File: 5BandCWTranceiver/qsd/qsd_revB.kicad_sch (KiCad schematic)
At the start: 56 parts, among them IC1 MCP1801, IC2 SN74LVC1G04DBVT, IC3 SN74AUP2G79DCUR, IC4 TS5A23157, IC5 SN74CBTLV3253, IC6 SN74LVC1G04DBVT, J1 Conn_Coaxial, J2 Conn_Coaxial, J3 Conn_Coaxial, Q1 J309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

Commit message: Update Audio Board
modify design and layout improvements
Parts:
- C12, C13, C14, C15: value 0.15uF -> 0.22uF
- R8: value 4.7k -> 4.32K
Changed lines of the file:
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@@
       (effects (font (size 1.778 1.5113)) (justify left bottom))
     )
-    (property "Value" "0.15uF" (id 1) (at 289.56 111.76 90)
+    (property "Value" "0.22uF" (id 1) (at 289.56 111.76 90)
       (effects (font (size 1.778 1.5113)) (justify left bottom))
     )
@@
       (effects (font (size 1.778 1.5113)) (justify left bottom))
     )
-    (property "Value" "0.15uF" (id 1) (at 274.32 111.76 90)
+    (property "Value" "0.22uF" (id 1) (at 274.32 111.76 90)
       (effects (font (size 1.778 1.5113)) (justify left bottom))
     )
@@
     (pin "2")
     (pin "3")
+    (pin "5")
+    (pin "6")
+    (pin "7")
+    (pin "4")
+    (pin "8")
   )
   (symbol (lib_id "qsd_revB-eagle-import:CAP0603-CAP") (at 264.16 134.62 180) (unit 1)
@@
       (effects (font (size 1.27 1.27)) hide)
     )
+    (pin "1")
+    (pin "2")
+    (pin "3")
     (pin "5")
     (pin "6")
     (pin "7")
+    (pin "4")
+    (pin "8")
   )
   (symbol (lib_id "qsd_revB-eagle-import:SN74LVC1G04DBVT") (at 111.76 167.64 0) (mirror y) (unit 1)
@@
       (effects (font (size 1.778 1.5113)) (justify left bottom))
     )
-    (property "Value" "0.15uF" (id 1) (at 297.18 111.76 90)
+    (property "Value" "0.22uF" (id 1) (at 297.18 111.76 90)
       (effects (font (size 1.778 1.5113)) (justify left bottom))
     )
@@
       (effects (font (size 1.778 1.5113)) (justify left bottom))
     )
-    (property "Value" "0.15uF" (id 1) (at 281.94 111.76 90)
+    (property "Value" "0.22uF" (id 1) (at 281.94 111.76 90)
       (effects (font (size 1.778 1.5113)) (justify left bottom))
     )
@@
       (effects (font (size 1.27 1.27)) hide)
     )
+    (pin "1")
+    (pin "2")
+    (pin "3")
+    (pin "5")
+    (pin "6")
+    (pin "7")
     (pin "4")
     (pin "8")
@@
       (effects (font (size 1.778 1.5113)) (justify left bottom))
     )
-    (property "Value" "4.7k" (id 1) (at 183.642 74.422 90)
+    (property "Value" "4.32K" (id 1) (at 183.642 74.422 90)
       (effects (font (size 1.778 1.5113)) (justify left bottom))
     )
@@
     )
     (path "/34e7dd80-c472-473e-a03d-21ea2317bbb8"
-      (reference "C12") (unit 1) (value "0.15uF") (footprint "Capacitor_SMD:C_0603_1608Metric_Pad1.08x0.95mm_HandSolder")
+      (reference "C12") (unit 1) (value "0.22uF") (footprint "Capacitor_SMD:C_0603_1608Metric_Pad1.08x0.95mm_HandSolder")
     )
     (path "/a8fd90c3-93bd-4d70-a767-e358a34a4f2a"
-      (reference "C13") (unit 1) (value "0.15uF") (footprint "Capacitor_SMD:C_0603_1608Metric_Pad1.08x0.95mm_HandSolder")
+      (reference "C13") (unit 1) (value "0.22uF") (footprint "Capacitor_SMD:C_0603_1608Metric_Pad1.08x0.95mm_HandSolder")
     )
     (path "/31c0c5d6-f2fd-4c78-836e-b4282fb318e1"
-      (reference "C14") (unit 1) (value "0.15uF") (footprint "Capacitor_SMD:C_0603_1608Metric_Pad1.08x0.95mm_HandSolder")
+      (reference "C14") (unit 1) (value "0.22uF") (footprint "Capacitor_SMD:C_0603_1608Metric_Pad1.08x0.95mm_HandSolder")
     )
     (path "/59cf1f4c-3c5e-4212-a0d9-c5ed9febcb10"
-      (reference "C15") (unit 1) (value "0.15uF") (footprint "Capacitor_SMD:C_0603_1608Metric_Pad1.08x0.95mm_HandSolder")
+      (reference "C15") (unit 1) (value "0.22uF") (footprint "Capacitor_SMD:C_0603_1608Metric_Pad1.08x0.95mm_HandSolder")
     )
     (path "/bac4bbf2-6a2f-46b1-b0c0-bf58806b4d24"
@@
     )
     (path "/ea505101-ccf9-4547-a897-6133e97a8a41"
-      (reference "R8") (unit 1) (value "4.7k") (footprint "Resistor_SMD:R_0603_1608Metric_Pad0.98x0.95mm_HandSolder")
+      (reference "R8") (unit 1) (value "4.32K") (footprint "Resistor_SMD:R_0603_1608Metric_Pad0.98x0.95mm_HandSolder")
     )
     (path "/e77cdba9-df1d-409f-b12f-bec7ebba09c1"

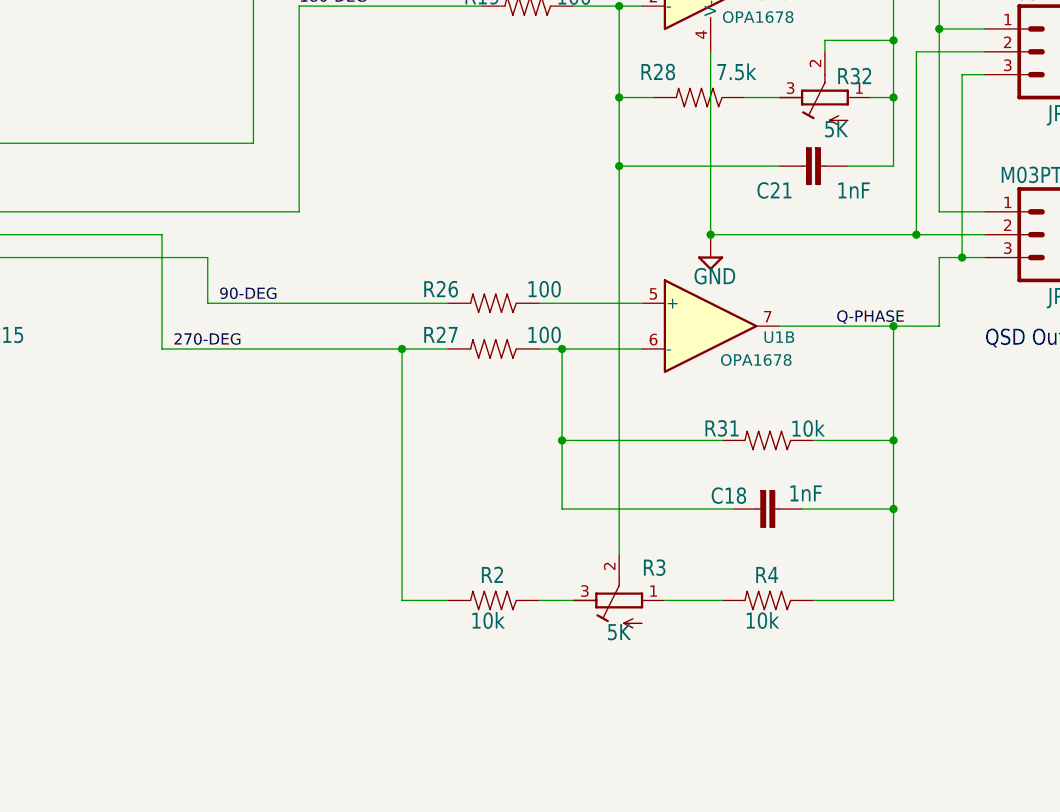
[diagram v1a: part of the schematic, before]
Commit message: Tapeout - audio and power boards
Last mods to audio board; new power board
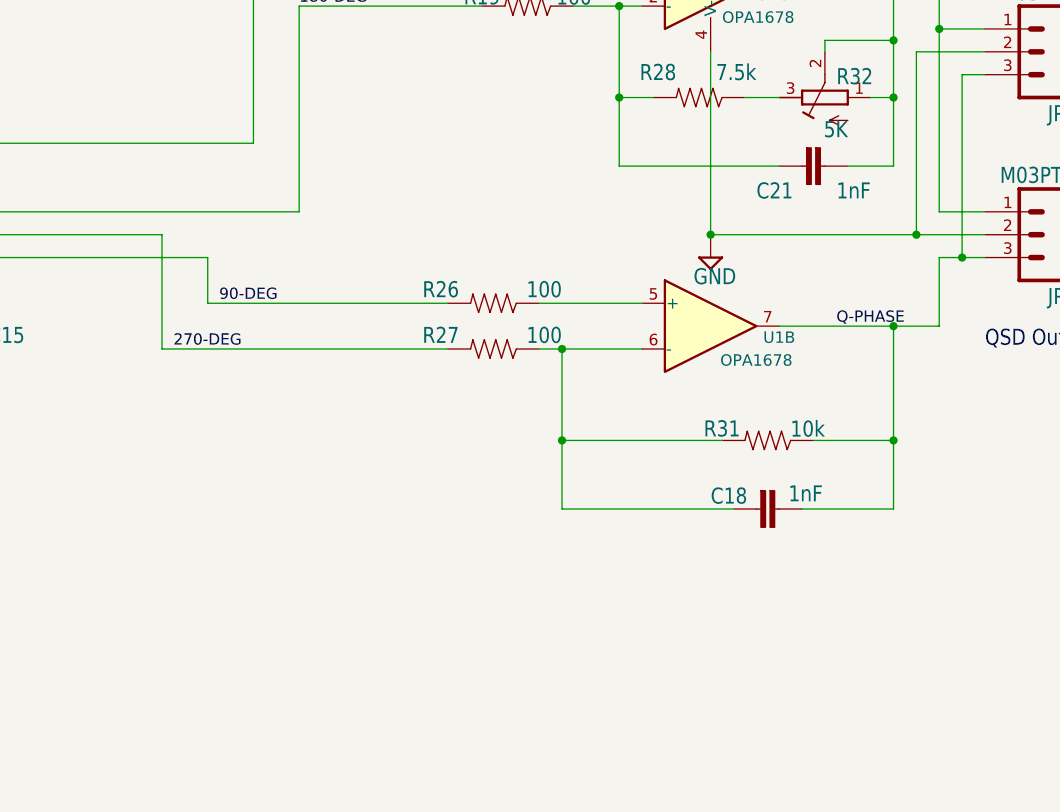
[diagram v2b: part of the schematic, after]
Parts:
- removed R2, R4: 10k, Resistor_SMD:R_0603_1608Metric_Pad0.98x0.95mm_HandSolder, symbol qsd_revB-eagle-import:RESISTOR0603-RES
- removed R3: 5K, qsd_revB:RTRIM3296W, symbol qsd_revB-eagle-import:R-TRIMM3296W
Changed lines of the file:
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@@
   (junction (at 116.84 154.94) (diameter 0) (color 0 0 0 0)
   )
-  (junction (at 368.3 88.9) (diameter 0) (color 0 0 0 0)
-  )
   (junction (at 152.4 139.7) (diameter 0) (color 0 0 0 0)
   )
@@
   (junction (at 266.7 83.82) (diameter 0) (color 0 0 0 0)
   )
-  (junction (at 398.78 127) (diameter 0) (color 0 0 0 0)
-  )
   (junction (at 398.78 106.68) (diameter 0) (color 0 0 0 0)
   )
@@
   (junction (at 274.32 86.36) (diameter 0) (color 0 0 0 0)
   )
-  (junction (at 344.17 109.22) (diameter 0) (color 0 0 0 0)
-  )
   (junction (at 45.72 33.02) (diameter 0) (color 0 0 0 0)
   )
@@
     (stroke (width 0) (type default) (color 0 0 0 0))
   )
-  (wire (pts (xy 368.3 88.9) (xy 368.3 132.08))
-    (stroke (width 0) (type default) (color 0 0 0 0))
-  )
   (wire (pts (xy 180.34 144.78) (xy 170.18 144.78))
     (stroke (width 0) (type default) (color 0 0 0 0))
@@
     (stroke (width 0) (type default) (color 0 0 0 0))
   )
-  (wire (pts (xy 359.41 137.16) (xy 363.22 137.16))
-    (stroke (width 0) (type default) (color 0 0 0 0))
-  )
   (wire (pts (xy 40.64 50.8) (xy 45.72 50.8))
     (stroke (width 0) (type default) (color 0 0 0 0))
@@
     (stroke (width 0) (type default) (color 0 0 0 0))
   )
-  (wire (pts (xy 373.38 137.16) (xy 379.73 137.16))
-    (stroke (width 0) (type default) (color 0 0 0 0))
-  )
   (wire (pts (xy 210.82 180.34) (xy 187.96 180.34))
     (stroke (width 0) (type default) (color 0 0 0 0))
@@
     (stroke (width 0) (type default) (color 0 0 0 0))
   )
-  (wire (pts (xy 317.5 109.22) (xy 344.17 109.22))
+  (wire (pts (xy 317.5 109.22) (xy 349.25 109.22))
     (stroke (width 0) (type default) (color 0 0 0 0))
   )
@@
     (stroke (width 0) (type default) (color 0 0 0 0))
   )
-  (wire (pts (xy 344.17 109.22) (xy 349.25 109.22))
-    (stroke (width 0) (type default) (color 0 0 0 0))
-  )
   (wire (pts (xy 147.32 144.78) (xy 154.94 144.78))
     (stroke (width 0) (type default) (color 0 0 0 0))
@@
     (stroke (width 0) (type default) (color 0 0 0 0))
   )
-  (wire (pts (xy 344.17 137.16) (xy 344.17 109.22))
-    (stroke (width 0) (type default) (color 0 0 0 0))
-  )
   (wire (pts (xy 105.41 208.28) (xy 105.41 193.04))
     (stroke (width 0) (type default) (color 0 0 0 0))
@@
     (stroke (width 0) (type default) (color 0 0 0 0))
   )
-  (wire (pts (xy 389.89 137.16) (xy 398.78 137.16))
-    (stroke (width 0) (type default) (color 0 0 0 0))
-  )
   (wire (pts (xy 266.7 93.98) (xy 264.16 93.98))
     (stroke (width 0) (type default) (color 0 0 0 0))
@@
     (stroke (width 0) (type default) (color 0 0 0 0))
   )
-  (wire (pts (xy 344.17 137.16) (xy 349.25 137.16))
-    (stroke (width 0) (type default) (color 0 0 0 0))
-  )
   (wire (pts (xy 398.78 106.68) (xy 386.08 106.68))
     (stroke (width 0) (type default) (color 0 0 0 0))
@@
   )
   (wire (pts (xy 403.86 45.72) (xy 403.86 48.26))
-    (stroke (width 0) (type default) (color 0 0 0 0))
-  )
-  (wire (pts (xy 398.78 137.16) (xy 398.78 127))
     (stroke (width 0) (type default) (color 0 0 0 0))
   )
@@
     (pin "2")
   )
-  (symbol (lib_id "qsd_revB-eagle-import:R-TRIMM3296W") (at 368.3 137.16 90) (unit 1)
-    (in_bom yes) (on_board yes)
-    (property "Reference" "R3" (id 0) (at 370.84 134.62 90)
-      (effects (font (size 1.778 1.5113)) (justify right top))
-    )
-    (property "Value" "5K" (id 1) (at 369.57 139.7 90)
-      (effects (font (size 1.778 1.5113)) (justify left bottom))
-    )
-    (property "Footprint" "qsd_revB:RTRIM3296W" (id 2) (at 368.3 137.16 0)
-      (effects (font (size 1.27 1.27)) hide)
-    )
-    (property "Datasheet" "" (id 3) (at 368.3 137.16 0)
-      (effects (font (size 1.27 1.27)) hide)
-    )
-    (pin "1")
-    (pin "2")
-    (pin "3")
-  )
   (symbol (lib_id "qsd_revB-eagle-import:GND") (at 45.72 88.9 0) (unit 1)
     (in_bom yes) (on_board yes)
@@
     (pin "2")
   )
-  (symbol (lib_id "qsd_revB-eagle-import:RESISTOR0603-RES") (at 384.81 137.16 180) (unit 1)
-    (in_bom yes) (on_board yes)
-    (property "Reference" "R4" (id 0) (at 386.08 133.35 0)
-      (effects (font (size 1.778 1.5113)) (justify left bottom))
-    )
-    (property "Value" "10k" (id 1) (at 386.08 138.43 0)
-      (effects (font (size 1.778 1.5113)) (justify left bottom))
-    )
-    (property "Footprint" "Resistor_SMD:R_0603_1608Metric_Pad0.98x0.95mm_HandSolder" (id 2) (at 384.81 137.16 0)
-      (effects (font (size 1.27 1.27)) hide)
-    )
-    (property "Datasheet" "" (id 3) (at 384.81 137.16 0)
-      (effects (font (size 1.27 1.27)) hide)
-    )
-    (pin "1")
-    (pin "2")
-  )
   (symbol (lib_id "qsd_revB-eagle-import:GND") (at 274.32 132.08 0) (unit 1)
     (in_bom yes) (on_board yes)
@@
     )
     (property "Datasheet" "" (id 3) (at 388.62 88.9 0)
-      (effects (font (size 1.27 1.27)) hide)
-    )
-    (pin "1")
-    (pin "2")
-  )
-  (symbol (lib_id "qsd_revB-eagle-import:RESISTOR0603-RES") (at 354.33 137.16 180) (unit 1)
-    (in_bom yes) (on_board yes)
-    (property "Reference" "R2" (id 0) (at 355.6 133.35 0)
-      (effects (font (size 1.778 1.5113)) (justify left bottom))
-    )
-    (property "Value" "10k" (id 1) (at 355.6 138.43 0)
-      (effects (font (size 1.778 1.5113)) (justify left bottom))
-    )
-    (property "Footprint" "Resistor_SMD:R_0603_1608Metric_Pad0.98x0.95mm_HandSolder" (id 2) (at 354.33 137.16 0)
-      (effects (font (size 1.27 1.27)) hide)
-    )
-    (property "Datasheet" "" (id 3) (at 354.33 137.16 0)
       (effects (font (size 1.27 1.27)) hide)
     )
@@
       (reference "R1") (unit 1) (value "0") (footprint "Resistor_SMD:R_0603_1608Metric_Pad0.98x0.95mm_HandSolder")
     )
-    (path "/d94d74ca-a0c7-466a-87bd-7c3cad1139e3"
-      (reference "R2") (unit 1) (value "10k") (footprint "Resistor_SMD:R_0603_1608Metric_Pad0.98x0.95mm_HandSolder")
-    )
-    (path "/6aef1be9-e827-4114-9ece-9d96d0349833"
-      (reference "R3") (unit 1) (value "5K") (footprint "qsd_revB:RTRIM3296W")
-    )
-    (path "/9d590871-64af-4172-9aa9-81c90999a09a"
-      (reference "R4") (unit 1) (value "10k") (footprint "Resistor_SMD:R_0603_1608Metric_Pad0.98x0.95mm_HandSolder")
-    )
     (path "/07d678ca-1c8c-46c9-aa5b-6d2a0679c45d"
